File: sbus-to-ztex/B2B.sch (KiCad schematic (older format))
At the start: 6 parts, among them J1 Conn_01x06_Male, J3 Conn_02x07_Odd_Even

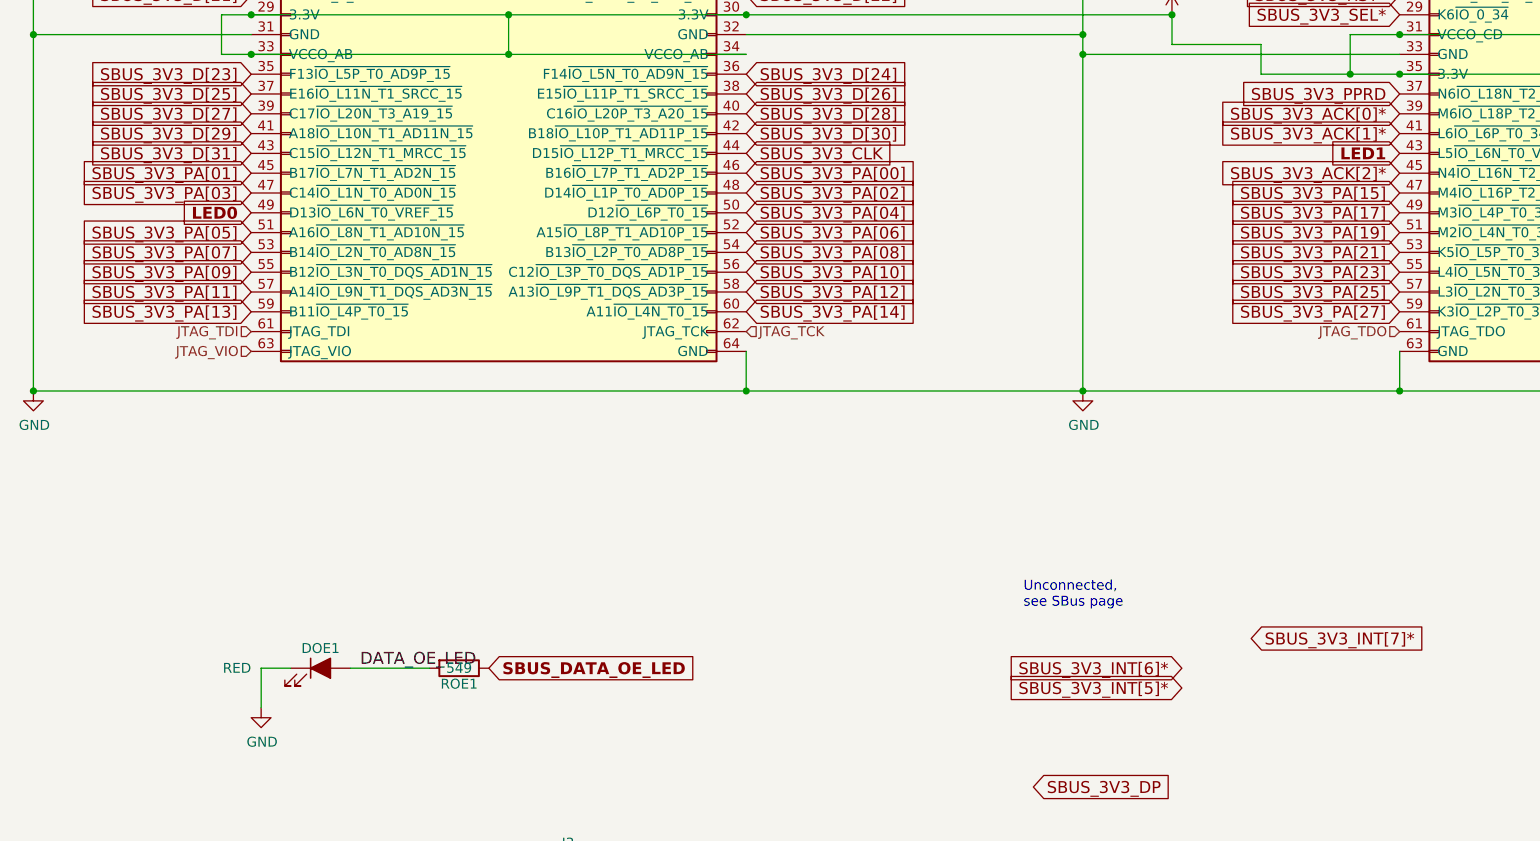
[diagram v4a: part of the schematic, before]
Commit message: Fewer LEDs, more interrupts, replace USB VBus power chip by something that might be available..., update signals file
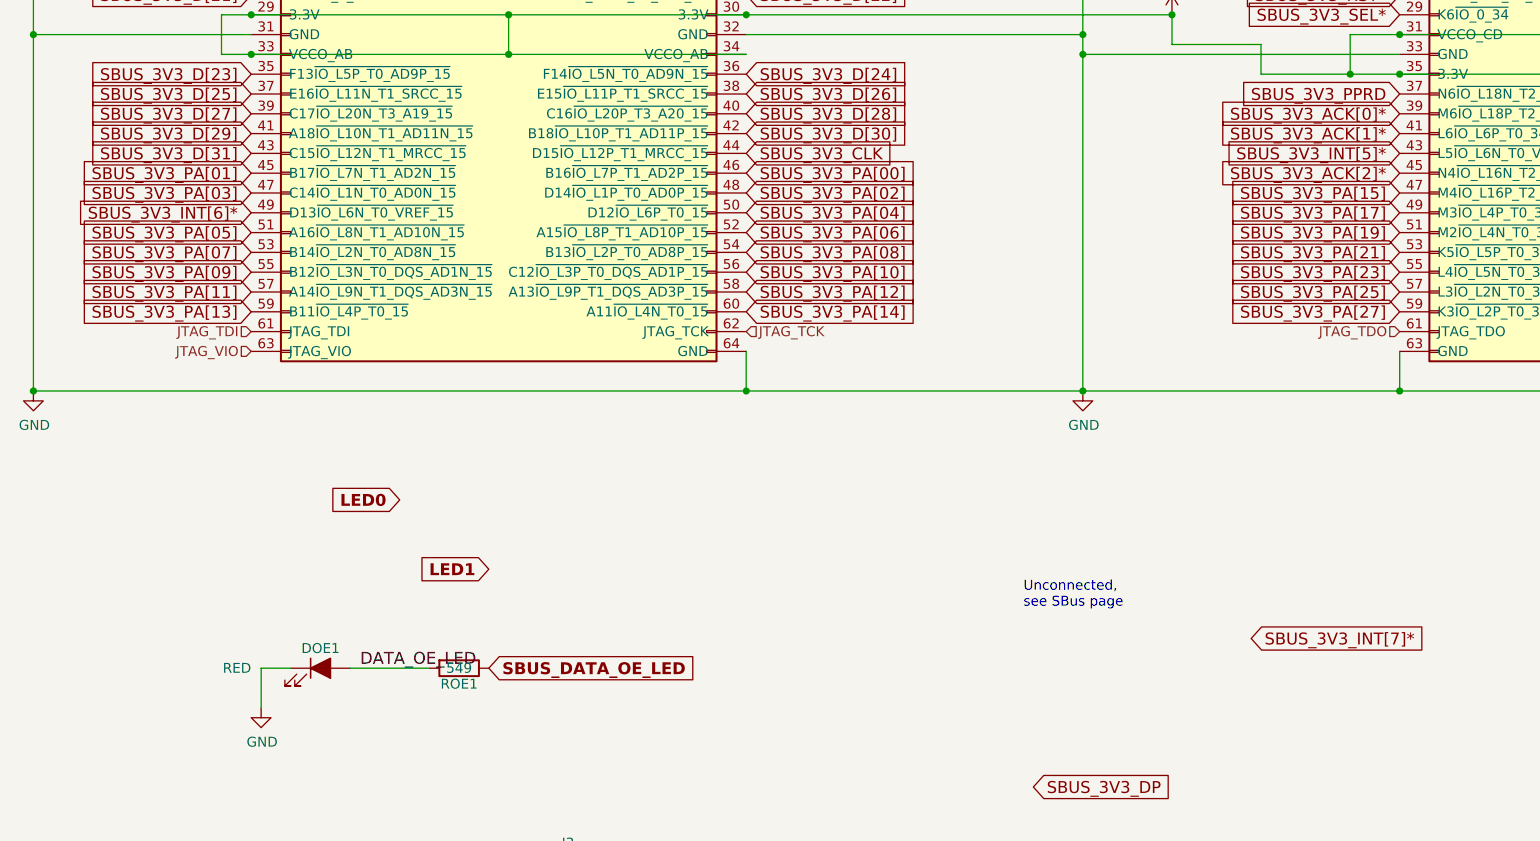
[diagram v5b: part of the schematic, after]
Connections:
- net LED0: no longer JAB1.49 (D13~IO_L6N_T0_VREF_15)
- net LED1: no longer JCD1.43 (L5~IO_L6N_T0_VREF_34)
- net SBUS_3V3_INT[5]*: now also JCD1.43 (L5~IO_L6N_T0_VREF_34)
- net SBUS_3V3_INT[6]*: now also JAB1.49 (D13~IO_L6N_T0_VREF_15)
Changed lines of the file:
@@
 Text GLabel 6650 5700 2    60   Input ~ 0
 SBUS_3V3_INT[7]*
-Text GLabel 6300 5850 0    60   Input ~ 0
+Text GLabel 1600 3550 0    60   Input ~ 0
 SBUS_3V3_INT[6]*
-Text GLabel 6300 5950 0    60   Input ~ 0
+Text GLabel 7400 3250 0    60   Input ~ 0
 SBUS_3V3_INT[5]*
 Text GLabel 9900 3050 2    60   Input ~ 0
@@
 Text GLabel 7400 1750 0    50   Input ~ 0
 PMOD-11
-Text GLabel 1600 3550 0    60   Input ~ 12
+Text GLabel 2350 5000 0    60   Input ~ 12
 LED0
-Text GLabel 7400 3250 0    60   Input ~ 12
+Text GLabel 2800 5350 0    60   Input ~ 12
 LED1
 $EndSCHEMATC

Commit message: Update more stuff to V1.2
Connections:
- net SBUS_3V3_EER*: now also JAB1.49 (D13~IO_L6N_T0_VREF_15); no longer JCD1.25 (V2~IO_L9N_T1_DQS_34)
- net SBUS_3V3_INT[6]*: now also JCD1.25 (V2~IO_L9N_T1_DQS_34); no longer JAB1.49 (D13~IO_L6N_T0_VREF_15)
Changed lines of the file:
@@
 Text GLabel 6650 5700 2    60   Input ~ 0
 SBUS_3V3_INT[7]*
-Text GLabel 1600 3550 0    60   Input ~ 0
+Text GLabel 7400 2350 0    60   Input ~ 0
 SBUS_3V3_INT[6]*
 Text GLabel 7400 3250 0    60   Input ~ 0
@@
 Text GLabel 7400 2950 0    60   Input ~ 0
 SBUS_3V3_PPRD
-Text GLabel 7400 2350 0    60   Input ~ 0
+Text GLabel 1600 3550 0    60   Input ~ 0
 SBUS_3V3_EER*
 Wire Wire Line

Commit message: thinking about a V1.3
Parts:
- removed DOE1: RED, LED_SMD:LED_0805_2012Metric, symbol Device:LED_ALT
- removed J1: Conn_01x06_Male, For_SeeedStudio:PinHeader_1x06_P2.54mm_Horizontal_For_SeeedStudio, symbol Connector:Conn_01x06_Male
- removed ROE1: 549, Resistor_SMD:R_0603_1608Metric, symbol Device:R
- added C24, C8: 100nF 0402, Capacitor_SMD:C_0402_1005Metric, symbol Device:C
- added C6: 47uF 0805, Capacitor_SMD:C_0805_2012Metric, symbol Device:C
- J3: DNP (none) -> DNP
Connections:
- net PMOD-10 is gone; now on net SD_D2: JCD1.42 (P4~IO_L14P_T2_SRCC_34)
- net PMOD-11 is gone; now on net SBUS_3V3_INT[5]*: JCD1.13 (T8~IO_L24N_T3_34)
- net PMOD-12 is gone; now on net SBUS_3V3_INT[4]*: JCD1.11 (U6~IO_L22N_T3_34)
- net PMOD-5 is gone; now on net SD_CLK: JCD1.48 (R1~IO_L17P_T2_34)
- net PMOD-6 is gone; now on net SBUS_3V3_D[23]: JCD1.28 (T3~IO_L11N_T1_SRCC_34)
- net PMOD-7 is gone; now on net SD_CMD: JCD1.46 (T1~IO_L17N_T2_34)
- net PMOD-9 is gone; now on net SD_D3: JCD1.44 (P3~IO_L14N_T2_SRCC_34)
- net RX is gone; now on net USBH0_D+: JCD1.5 (U9~IO_L21P_T3_DQS_34)
- net SBUS_DATA_OE_LED is gone; now on net SBUS_3V3_D[17]: JCD1.26 (U1~IO_L7P_T1_34)
- net TX is gone; now on net USBH0_D-: JCD1.6 (V9~IO_L21N_T3_DQS_34)
- net +3V3: now also C24.1, C8.1
- net +5V: now also C6.1
- net GND: now also C24.2, C6.2, C8.2
- net SBUS_3V3_ACK[0]*: now also JAB1.48 (D14~IO_L1P_T0_AD0P_15); no longer JCD1.39 (M6~IO_L18P_T2_34)
- net SBUS_3V3_ACK[1]*: now also JCD1.56 (N1~IO_L3N_T0_DQS_34); no longer JCD1.41 (L6~IO_L6P_T0_34)
- net SBUS_3V3_ACK[2]*: now also JAB1.57 (A14~IO_L9N_T1_DQS_AD3N_15); no longer JCD1.45 (N4~IO_L16N_T2_34)
- net SBUS_3V3_AS*: now also JAB1.11 (H15~IO_L19N_T3_A21_VREF_15); no longer JCD1.18 (T4~IO_L12N_T1_MRCC_34)
- net SBUS_3V3_BG*: now also JAB1.7 (K15~IO_L24P_T3_RS1_15); no longer JCD1.17 (R7~IO_L23P_T3_34)
- net SBUS_3V3_BR*: now also JAB1.5 (K16~IO_25_15); no longer JCD1.21 (R6~IO_L19P_T3_34)
- net SBUS_3V3_CLK: now also JAB1.20 (H16~IO_L13P_T2_MRCC_15); no longer JAB1.44 (D15~IO_L12P_T1_MRCC_15)
- net SBUS_3V3_D[00]: now also JCD1.17 (R7~IO_L23P_T3_34); no longer JAB1.6 (J18~IO_L23N_T3_FWE_B_15)
- net SBUS_3V3_D[01]: now also JAB1.13 (J14~IO_L19P_T3_A22_15); no longer JAB1.5 (K16~IO_25_15)
- net SBUS_3V3_D[02]: now also JAB1.14 (H14~IO_L15P_T2_DQS_15); no longer JAB1.8 (J17~IO_L23P_T3_FOE_B_15)
- net SBUS_3V3_D[03]: now also JCD1.19 (T6~IO_L23N_T3_34); no longer JAB1.7 (K15~IO_L24P_T3_RS1_15)
- net SBUS_3V3_D[04]: now also JAB1.15 (H17~IO_L18P_T2_A24_15); no longer JAB1.10 (K13~IO_L17P_T2_A26_15)
- net SBUS_3V3_D[05]: now also JAB1.16 (G14~IO_L15N_T2_DQS_ADV_B_15); no longer JAB1.9 (J15~IO_L24N_T3_RS0_15)
- net SBUS_3V3_D[06]: now also JCD1.21 (R6~IO_L19P_T3_34); no longer JAB1.12 (J13~IO_L17N_T2_A25_15)
- net SBUS_3V3_D[07]: now also JAB1.17 (G17~IO_L18N_T2_A23_15); no longer JAB1.13 (J14~IO_L19P_T3_A22_15)
- net SBUS_3V3_D[08]: now also JAB1.18 (G16~IO_L13N_T2_MRCC_15); no longer JAB1.14 (H14~IO_L15P_T2_DQS_15)
- net SBUS_3V3_D[09]: now also JCD1.23 (R5~IO_L19N_T3_VREF_34); no longer JAB1.15 (H17~IO_L18P_T2_A24_15)
- net SBUS_3V3_D[10]: now also JAB1.19 (G18~IO_L22P_T3_A17_15); no longer JAB1.16 (G14~IO_L15N_T2_DQS_ADV_B_15)
- net SBUS_3V3_D[11]: now also JCD1.24 (V1~IO_L7N_T1_34); no longer JAB1.17 (G17~IO_L18N_T2_A23_15)
- net SBUS_3V3_D[12]: now also JAB1.21 (F18~IO_L22N_T3_A16_15); no longer JAB1.18 (G16~IO_L13N_T2_MRCC_15)
- net SBUS_3V3_D[13]: now also JAB1.22 (F16~IO_L14N_T2_SRCC_15); no longer JAB1.19 (G18~IO_L22P_T3_A17_15)
- net SBUS_3V3_D[14]: now also JCD1.25 (V2~IO_L9N_T1_DQS_34); no longer JAB1.20 (H16~IO_L13P_T2_MRCC_15)
- net SBUS_3V3_D[15]: now also JAB1.23 (E18~IO_L21P_T3_DQS_15); no longer JAB1.21 (F18~IO_L22N_T3_A16_15)
- net SBUS_3V3_D[16]: now also JAB1.24 (F15~IO_L14P_T2_SRCC_15); no longer JAB1.22 (F16~IO_L14N_T2_SRCC_15)
- net SBUS_3V3_D[17]: no longer JAB1.23 (E18~IO_L21P_T3_DQS_15)
- net SBUS_3V3_D[18]: now also JAB1.25 (D18~IO_L21N_T3_DQS_A18_15); no longer JAB1.24 (F15~IO_L14P_T2_SRCC_15)
- net SBUS_3V3_D[19]: now also JAB1.26 (E17~IO_L16P_T2_A28_15); no longer JAB1.25 (D18~IO_L21N_T3_DQS_A18_15)
- net SBUS_3V3_D[20]: now also JCD1.27 (U2~IO_L9P_T1_DQS_34); no longer JAB1.26 (E17~IO_L16P_T2_A28_15)
- net SBUS_3V3_D[23]: no longer JAB1.35 (F13~IO_L5P_T0_AD9P_15)
- net SBUS_3V3_D[24]: now also JCD1.29 (K6~IO_0_34); no longer JAB1.36 (F14~IO_L5N_T0_AD9N_15)
- net SBUS_3V3_D[25]: now also JCD1.30 (R3~IO_L11P_T1_SRCC_34); no longer JAB1.37 (E16~IO_L11N_T1_SRCC_15)
- net SBUS_3V3_D[26]: now also JCD1.38 (P5~IO_L13N_T2_MRCC_34); no longer JAB1.38 (E15~IO_L11P_T1_SRCC_15)
- net SBUS_3V3_D[27]: now also JCD1.37 (N6~IO_L18N_T2_34); no longer JAB1.39 (C17~IO_L20N_T3_A19_15)
- net SBUS_3V3_D[28]: now also JCD1.39 (M6~IO_L18P_T2_34); no longer JAB1.40 (C16~IO_L20P_T3_A20_15)
- net SBUS_3V3_D[29]: now also JCD1.41 (L6~IO_L6P_T0_34); no longer JAB1.41 (A18~IO_L10N_T1_AD11N_15)
- net SBUS_3V3_D[30]: now also JAB1.35 (F13~IO_L5P_T0_AD9P_15); no longer JAB1.42 (B18~IO_L10P_T1_AD11P_15)
- net SBUS_3V3_D[31]: now also JAB1.36 (F14~IO_L5N_T0_AD9N_15); no longer JAB1.43 (C15~IO_L12N_T1_MRCC_15)
- net SBUS_3V3_EER*: now also JAB1.43 (C15~IO_L12N_T1_MRCC_15); no longer JAB1.49 (D13~IO_L6N_T0_VREF_15)
- net SBUS_3V3_INT[1]*: now also JAB1.9 (J15~IO_L24N_T3_RS0_15); no longer JCD1.23 (R5~IO_L19N_T3_VREF_34)
- net SBUS_3V3_INT[2]*: now also JCD1.7 (U8~IO_25_34); no longer JAB1.11 (H15~IO_L19N_T3_A21_VREF_15)
- net SBUS_3V3_INT[3]*: now also JCD1.9 (U7~IO_L22P_T3_34); no longer JCD1.30 (R3~IO_L11P_T1_SRCC_34)
- net SBUS_3V3_INT[4]*: no longer JCD1.40 (N5~IO_L13P_T2_MRCC_34)
- net SBUS_3V3_INT[5]*: no longer JCD1.43 (L5~IO_L6N_T0_VREF_34)
- net SBUS_3V3_INT[6]*: now also JCD1.15 (R8~IO_L24P_T3_34); no longer JCD1.25 (V2~IO_L9N_T1_DQS_34)
- net SBUS_3V3_PA[00]: now also JAB1.40 (C16~IO_L20P_T3_A20_15); no longer JAB1.46 (B16~IO_L7P_T1_AD2P_15)
- net SBUS_3V3_PA[01]: now also JAB1.39 (C17~IO_L20N_T3_A19_15); no longer JAB1.45 (B17~IO_L7N_T1_AD2N_15)
- net SBUS_3V3_PA[02]: now also JAB1.41 (A18~IO_L10N_T1_AD11N_15); no longer JAB1.48 (D14~IO_L1P_T0_AD0P_15)
- net SBUS_3V3_PA[03]: now also JCD1.47 (M4~IO_L16P_T2_34); no longer JAB1.47 (C14~IO_L1N_T0_AD0N_15)
- net SBUS_3V3_PA[04]: now also JCD1.49 (M3~IO_L4P_T0_34); no longer JAB1.50 (D12~IO_L6P_T0_15)
- net SBUS_3V3_PA[05]: now also JAB1.42 (B18~IO_L10P_T1_AD11P_15); no longer JAB1.51 (A16~IO_L8N_T1_AD10N_15)
- net SBUS_3V3_PA[06]: now also JCD1.51 (M2~IO_L4N_T0_34); no longer JAB1.52 (A15~IO_L8P_T1_AD10P_15)
- net SBUS_3V3_PA[07]: now also JAB1.44 (D15~IO_L12P_T1_MRCC_15); no longer JAB1.53 (B14~IO_L2N_T0_AD8N_15)
- net SBUS_3V3_PA[08]: now also JAB1.46 (B16~IO_L7P_T1_AD2P_15); no longer JAB1.54 (B13~IO_L2P_T0_AD8P_15)
- net SBUS_3V3_PA[09]: now also JAB1.45 (B17~IO_L7N_T1_AD2N_15); no longer JAB1.55 (B12~IO_L3N_T0_DQS_AD1N_15)
- net SBUS_3V3_PA[10]: now also JAB1.47 (C14~IO_L1N_T0_AD0N_15); no longer JAB1.56 (C12~IO_L3P_T0_DQS_AD1P_15)
- net SBUS_3V3_PA[11]: now also JCD1.53 (K5~IO_L5P_T0_34); no longer JAB1.57 (A14~IO_L9N_T1_DQS_AD3N_15)
- net SBUS_3V3_PA[12]: now also JAB1.49 (D13~IO_L6N_T0_VREF_15); no longer JAB1.58 (A13~IO_L9P_T1_DQS_AD3P_15)
- net SBUS_3V3_PA[13]: now also JCD1.54 (N2~IO_L3P_T0_DQS_34); no longer JAB1.59 (B11~IO_L4P_T0_15)
- net SBUS_3V3_PA[14]: now also JCD1.55 (L4~IO_L5N_T0_34); no longer JAB1.60 (A11~IO_L4N_T0_15)
- net SBUS_3V3_PA[15]: now also JAB1.50 (D12~IO_L6P_T0_15); no longer JCD1.47 (M4~IO_L16P_T2_34)
- net SBUS_3V3_PA[16]: now also JAB1.52 (A15~IO_L8P_T1_AD10P_15); no longer JCD1.50 (R2~IO_L15N_T2_DQS_34)
- net SBUS_3V3_PA[17]: now also JAB1.51 (A16~IO_L8N_T1_AD10N_15); no longer JCD1.49 (M3~IO_L4P_T0_34)
- net SBUS_3V3_PA[18]: now also JAB1.54 (B13~IO_L2P_T0_AD8P_15); no longer JCD1.52 (P2~IO_L15P_T2_DQS_34)
- net SBUS_3V3_PA[19]: now also JAB1.53 (B14~IO_L2N_T0_AD8N_15); no longer JCD1.51 (M2~IO_L4N_T0_34)
- net SBUS_3V3_PA[20]: now also JAB1.55 (B12~IO_L3N_T0_DQS_AD1N_15); no longer JCD1.54 (N2~IO_L3P_T0_DQS_34)
- net SBUS_3V3_PA[21]: now also JCD1.57 (L3~IO_L2N_T0_34); no longer JCD1.53 (K5~IO_L5P_T0_34)
- net SBUS_3V3_PA[22]: now also JCD1.58 (M1~IO_L1N_T0_34); no longer JCD1.56 (N1~IO_L3N_T0_DQS_34)
- net SBUS_3V3_PA[23]: now also JAB1.56 (C12~IO_L3P_T0_DQS_AD1P_15); no longer JCD1.55 (L4~IO_L5N_T0_34)
- net SBUS_3V3_PA[24]: now also JCD1.59 (K3~IO_L2P_T0_34); no longer JCD1.58 (M1~IO_L1N_T0_34)
- net SBUS_3V3_PA[25]: now also JAB1.58 (A13~IO_L9P_T1_DQS_AD3P_15); no longer JCD1.57 (L3~IO_L2N_T0_34)
- net SBUS_3V3_PA[26]: now also JAB1.60 (A11~IO_L4N_T0_15); no longer JCD1.60 (L1~IO_L1P_T0_34)
- net SBUS_3V3_PA[27]: now also JAB1.59 (B11~IO_L4P_T0_15); no longer JCD1.59 (K3~IO_L2P_T0_34)
- net SBUS_3V3_PPRD: now also JAB1.38 (E15~IO_L11P_T1_SRCC_15); no longer JCD1.37 (N6~IO_L18N_T2_34)
- net SBUS_3V3_RST*: now also JCD1.60 (L1~IO_L1P_T0_34); no longer JCD1.27 (U2~IO_L9P_T1_DQS_34)
- net SBUS_3V3_SEL*: now also JAB1.12 (J13~IO_L17N_T2_A25_15); no longer JCD1.29 (K6~IO_0_34)
- net SBUS_3V3_SIZ[0]: now also JAB1.37 (E16~IO_L11N_T1_SRCC_15); no longer JCD1.19 (T6~IO_L23N_T3_34)
- net SBUS_3V3_SIZ[1]: now also JCD1.43 (L5~IO_L6N_T0_VREF_34); no longer JCD1.22 (U3~IO_L8N_T1_34)
- net SBUS_3V3_SIZ[2]: now also JCD1.45 (N4~IO_L16N_T2_34); no longer JCD1.24 (V1~IO_L7N_T1_34)
- net SBUS_OE: now also JAB1.10 (K13~IO_L17P_T2_A26_15); no longer JCD1.38 (P5~IO_L13N_T2_MRCC_34)
- net SD_CLK: no longer JCD1.15 (R8~IO_L24P_T3_34)
- net SD_CMD: no longer JCD1.16 (T5~IO_L12P_T1_MRCC_34)
- net SD_D0: now also JCD1.50 (R2~IO_L15N_T2_DQS_34); no longer JCD1.12 (V5~IO_L10P_T1_34)
- net SD_D1: now also JCD1.52 (P2~IO_L15P_T2_DQS_34); no longer JCD1.14 (V4~IO_L10N_T1_34)
- net SD_D2: no longer JCD1.8 (V7~IO_L20P_T3_34)
- net SD_D3: no longer JCD1.10 (V6~IO_L20N_T3_34)
- net USBH0_D+: no longer JCD1.7 (U8~IO_25_34)
- net USBH0_D-: no longer JCD1.9 (U7~IO_L22P_T3_34)
- net PMOD-8 renamed HDMI_CLK+
- new net CLK_54_000: JCD1.40 (N5~IO_L13P_T2_MRCC_34)
- new net HDMI_CLK-: JCD1.22 (U3~IO_L8N_T1_34)
- new net HDMI_D0+: JCD1.16 (T5~IO_L12P_T1_MRCC_34)
- new net HDMI_D0-: JCD1.18 (T4~IO_L12N_T1_MRCC_34)
- new net HDMI_D1+: JCD1.12 (V5~IO_L10P_T1_34)
- new net HDMI_D1-: JCD1.14 (V4~IO_L10N_T1_34)
- new net HDMI_D2+: JCD1.8 (V7~IO_L20P_T3_34)
- new net HDMI_D2-: JCD1.10 (V6~IO_L20N_T3_34)
- new net I2C0_SCL: JAB1.8 (J17~IO_L23P_T3_FOE_B_15)
- new net I2C0_SDA: JAB1.6 (J18~IO_L23N_T3_FWE_B_15)
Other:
- note removed: "Unconnected,\nsee SBus page"

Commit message: more V1.3
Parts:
- JAB1, JCD1: DNP (none) -> DNP
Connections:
- net labels added: PMOD-1112+, PMOD-1112-, PMOD-56+, PMOD-56-, PMOD-78+, PMOD-78-, PMOD-910+, PMOD-910-
- net labels removed: SBUS_3V3_INT[1]*, SBUS_3V3_INT[6]*
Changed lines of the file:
@@
 F 4 "10-89-7642" H 1800 2650 50  0001 C CNN "MPN"
 F 5 "https://www2.mouser.com/ProductDetail/Molex/10-89-7642?qs=%2Fha2pyFadugCxzQFZUdvioDcljDVidgd4vXrOFuSRYM%3D" H 1800 2650 50  0001 C CNN "URL"
+F 6 "DNP" H 1800 2650 50  0001 C CNN "DNP"
 	1    1800 2650
 	1    0    0    -1
@@
 Text Notes 9950 6500 0    50   ~ 0
 Clock capable inputs (MRCC and SRCC, MRCC are multi-domain)\nFor 2.13:\nB9 G16~IO_L13N_T2_MRCC_15 G16\nB10 H16~IO_L13P_T2_MRCC_15 H16\nB11 F16~IO_L14N_T2_SRCC_15 F16\nB12 F15~IO_L14P_T2_SRCC_15 F15\nA19 E16~IO_L11N_T1_SRCC_15 E16\nB19 E15~IO_L11P_T1_SRCC_15 E15\nA22 C15~IO_L12N_T1_MRCC_15 C15\nB22 D15~IO_L12P_T1_MRCC_15 D15\nD8 T5~IO_L12P_T1_MRCC_34 T5\nD9 T4~IO_L12N_T1_MRCC_34 T4\nD14 T3~IO_L11N_T1_SRCC_34 T3\nD15 R3~IO_L11P_T1_SRCC_34 R3\nD19 P5~IO_L13N_T2_MRCC_34 P5\nD20 N5~IO_L13P_T2_MRCC_34 N5\nD21 P4~IO_L14P_T2_SRCC_34 P4\nD22 P3~IO_L14N_T2_SRCC_34 P3\n\nUnfortunately various 2.1x modules have different clock assignment. B22 hsould be a P-side MRCC for 2.14 (perhaps 2.18), but is a n-side SRCC on 2.16 so not usable there.
-Text GLabel 4100 2050 2    60   Input ~ 0
-SBUS_3V3_CLK
 Wire Wire Line
 	1450 2550 1450 2750
@@
 Wire Wire Line
 	7150 2850 6700 2850
-Text GLabel 7400 1950 0    60   Input ~ 0
-SBUS_3V3_D[00]
-Text GLabel 1600 1750 0    60   Input ~ 0
-SBUS_3V3_D[01]
-Text GLabel 4100 1750 2    60   Input ~ 0
-SBUS_3V3_D[02]
-Text GLabel 7400 2050 0    60   Input ~ 0
-SBUS_3V3_D[03]
-Text GLabel 1600 1850 0    60   Input ~ 0
-SBUS_3V3_D[04]
-Text GLabel 4100 1850 2    60   Input ~ 0
-SBUS_3V3_D[05]
-Text GLabel 7400 2150 0    60   Input ~ 0
-SBUS_3V3_D[06]
-Text GLabel 1600 1950 0    60   Input ~ 0
-SBUS_3V3_D[07]
+Text GLabel 1600 2150 0    60   Input ~ 0
+SBUS_3V3_D[14]
+Text GLabel 4100 1950 2    60   Input ~ 0
+SBUS_3V3_D[09]
+Text GLabel 1600 2050 0    60   Input ~ 0
+SBUS_3V3_D[11]
 Text GLabel 1600 2250 0    60   Input ~ 0
-SBUS_3V3_D[15]
-Text GLabel 7400 2350 0    60   Input ~ 0
-SBUS_3V3_D[14]
-Text GLabel 4100 2150 2    60   Input ~ 0
-SBUS_3V3_D[13]
-Text GLabel 1600 2150 0    60   Input ~ 0
-SBUS_3V3_D[12]
-Text GLabel 7400 2250 0    60   Input ~ 0
-SBUS_3V3_D[09]
-Text GLabel 4100 1950 2    60   Input ~ 0
-SBUS_3V3_D[08]
-Text GLabel 9900 2250 2    60   Input ~ 0
-SBUS_3V3_D[11]
-Text GLabel 1600 2050 0    60   Input ~ 0
-SBUS_3V3_D[10]
-Text GLabel 4100 2250 2    60   Input ~ 0
-SBUS_3V3_D[16]
-Text GLabel 9900 2350 2    60   Input ~ 0
 SBUS_3V3_D[17]
 Text GLabel 1600 2350 0    60   Input ~ 0
-SBUS_3V3_D[18]
-Text GLabel 4100 2350 2    60   Input ~ 0
-SBUS_3V3_D[19]
-Text GLabel 7400 2450 0    60   Input ~ 0
 SBUS_3V3_D[20]
 Text GLabel 1600 2450 0    60   Input ~ 0
-SBUS_3V3_D[21]
-Text GLabel 4100 2450 2    60   Input ~ 0
-SBUS_3V3_D[22]
-Text GLabel 9900 2450 2    60   Input ~ 0
 SBUS_3V3_D[23]
 Text GLabel 4100 2850 2    60   Input ~ 0
@@
 Text GLabel 1600 2850 0    60   Input ~ 0
 SBUS_3V3_D[30]
-Text GLabel 7400 3150 0    60   Input ~ 0
+Text GLabel 9900 2950 2    60   Input ~ 0
 SBUS_3V3_D[29]
-Text GLabel 7400 3050 0    60   Input ~ 0
-SBUS_3V3_D[28]
-Text GLabel 7400 2950 0    60   Input ~ 0
+Text GLabel 9900 2550 2    60   Input ~ 0
 SBUS_3V3_D[27]
-Text GLabel 9900 2950 2    60   Input ~ 0
+Text GLabel 7400 2550 0    60   Input ~ 0
 SBUS_3V3_D[26]
-Text GLabel 9900 2550 2    60   Input ~ 0
+Text GLabel 9900 2450 2    60   Input ~ 0
 SBUS_3V3_D[25]
-Text GLabel 7400 2550 0    60   Input ~ 0
+Text GLabel 4100 2450 2    60   Input ~ 0
 SBUS_3V3_D[24]
-Text GLabel 7400 1850 0    60   Input ~ 0
-SBUS_3V3_INT[6]*
 Text GLabel 7400 1750 0    60   Input ~ 0
 SBUS_3V3_INT[5]*
@@
 Text GLabel 7400 1450 0    60   Input ~ 0
 SBUS_3V3_INT[2]*
-Text GLabel 1600 1550 0    60   Input ~ 0
-SBUS_3V3_INT[1]*
 Text GLabel 4100 3050 2    60   Input ~ 0
 SBUS_3V3_PA[00]
@@
 Text GLabel 1600 3150 0    60   Input ~ 0
 SBUS_3V3_PA[02]
+Text GLabel 7400 3250 0    60   Input ~ 0
+SBUS_3V3_PA[03]
+Text GLabel 7400 3350 0    60   Input ~ 0
+SBUS_3V3_PA[04]
 Text GLabel 7400 3450 0    60   Input ~ 0
-SBUS_3V3_PA[03]
-Text GLabel 7400 3550 0    60   Input ~ 0
-SBUS_3V3_PA[04]
-Text GLabel 7400 3650 0    60   Input ~ 0
 SBUS_3V3_PA[06]
 Text GLabel 4100 3250 2    60   Input ~ 0
@@
 Text GLabel 4100 3550 2    60   Input ~ 0
 SBUS_3V3_PA[15]
-Text GLabel 7400 3850 0    60   Input ~ 0
+Text GLabel 7400 3750 0    60   Input ~ 0
 SBUS_3V3_PA[14]
-Text GLabel 9900 3750 2    60   Input ~ 0
+Text GLabel 7400 3650 0    60   Input ~ 0
 SBUS_3V3_PA[13]
 Text GLabel 1600 3550 0    60   Input ~ 0
 SBUS_3V3_PA[12]
-Text GLabel 7400 3750 0    60   Input ~ 0
+Text GLabel 7400 3550 0    60   Input ~ 0
 SBUS_3V3_PA[11]
 Text GLabel 1600 3450 0    60   Input ~ 0
@@
 Text GLabel 1600 2950 0    60   Input ~ 0
 SBUS_3V3_SIZ[0]
-Text GLabel 7400 3250 0    60   Input ~ 0
+Text GLabel 7400 3050 0    60   Input ~ 0
 SBUS_3V3_SIZ[1]
-Text GLabel 7400 3350 0    60   Input ~ 0
+Text GLabel 7400 3150 0    60   Input ~ 0
 SBUS_3V3_SIZ[2]
 Text GLabel 1600 1350 0    60   Input ~ 0
 SBUS_3V3_BR*
-Text GLabel 4100 1650 2    60   Input ~ 0
-SBUS_3V3_SEL*
 Text GLabel 1600 1450 0    60   Input ~ 0
 SBUS_3V3_BG*
-Text GLabel 1600 1650 0    60   Input ~ 0
-SBUS_3V3_AS*
 Text GLabel 1600 3950 0    60   Input ~ 0
 SBUS_3V3_ACK[2]*
-Text GLabel 9900 3850 2    60   Input ~ 0
+Text GLabel 7400 3850 0    60   Input ~ 0
 SBUS_3V3_ACK[1]*
 Text GLabel 4100 3450 2    60   Input ~ 0
@@
 Text GLabel 1600 3250 0    60   Input ~ 0
 SBUS_3V3_EER*
-Text GLabel 9900 3150 2    60   Input ~ 0
+Text GLabel 12225 3225 2    60   Input ~ 0
 SD_D2
-Text GLabel 9900 3250 2    60   Input ~ 0
+Text GLabel 12225 3325 2    60   Input ~ 0
 SD_D3
-Text GLabel 9900 3350 2    60   Input ~ 0
+Text GLabel 12225 3425 2    60   Input ~ 0
 SD_CMD
-Text GLabel 9900 3450 2    60   Input ~ 0
+Text GLabel 12225 3525 2    60   Input ~ 0
 SD_CLK
-Text GLabel 9900 3550 2    60   Input ~ 0
+Text GLabel 12225 3625 2    60   Input ~ 0
 SD_D0
-Text GLabel 9900 3650 2    60   Input ~ 0
+Text GLabel 12225 3725 2    60   Input ~ 0
 SD_D1
 $Comp
@@
 F 4 "10-89-7642" H 7600 2650 50  0001 C CNN "MPN"
 F 5 "https://www2.mouser.com/ProductDetail/Molex/10-89-7642?qs=%2Fha2pyFadugCxzQFZUdvioDcljDVidgd4vXrOFuSRYM%3D" H 7600 2650 50  0001 C CNN "URL"
+F 6 "DNP" H 7600 2650 50  0001 C CNN "DNP"
 	1    7600 2650
 	1    0    0    -1
@@
 Wire Wire Line
 	500  2650 1600 2650
-Wire Wire Line
-	1600 1250 4100 1250
-Wire Wire Line
-	1600 1250 500  1250
 Wire Wire Line
 	500  1250 500  2650
@@
 Text GLabel 9900 3050 2    50   Input Italic 0
 CLK_54_000
+Wire Wire Line
+	1600 1250 550  1250
+Wire Wire Line
+	1600 1250 4100 1250
+Text GLabel 1600 1550 0    60   Input ~ 0
+SBUS_3V3_AS*
+Text GLabel 4100 2350 2    60   Input ~ 0
+SBUS_3V3_D[21]
+Text GLabel 4100 2250 2    60   Input ~ 0
+SBUS_3V3_D[18]
+Text GLabel 7400 2150 0    60   Input ~ 0
+SBUS_3V3_D[10]
+Text GLabel 7400 2250 0    60   Input ~ 0
+SBUS_3V3_D[12]
+Text GLabel 4100 2150 2    60   Input ~ 0
+SBUS_3V3_D[15]
+Text GLabel 7400 2050 0    60   Input ~ 0
+SBUS_3V3_D[07]
+Text GLabel 7400 1950 0    60   Input ~ 0
+SBUS_3V3_D[04]
+Text GLabel 7400 1850 0    60   Input ~ 0
+SBUS_3V3_D[01]
+Text GLabel 7400 2950 0    60   Input ~ 0
+SBUS_3V3_D[28]
+Text GLabel 1600 1650 0    60   Input ~ 0
+SBUS_3V3_SEL*
+Text GLabel 7400 2450 0    60   Input ~ 0
+SBUS_3V3_D[22]
+Text GLabel 9900 2350 2    60   Input ~ 0
+SBUS_3V3_D[19]
+Text GLabel 7400 2350 0    60   Input ~ 0
+SBUS_3V3_D[16]
+Text GLabel 9900 2250 2    60   Input ~ 0
+SBUS_3V3_D[13]
+Text GLabel 1600 1850 0    60   Input ~ 0
+SBUS_3V3_D[05]
+Text GLabel 1600 1750 0    60   Input ~ 0
+SBUS_3V3_D[02]
+Text GLabel 4100 2050 2    60   Input ~ 0
+SBUS_3V3_CLK
+Text GLabel 1600 1950 0    60   Input ~ 0
+SBUS_3V3_D[08]
+Text GLabel 4100 1850 2    60   Input ~ 0
+SBUS_3V3_D[06]
+Text GLabel 4100 1750 2    60   Input ~ 0
+SBUS_3V3_D[03]
+Text GLabel 4100 1650 2    60   Input ~ 0
+SBUS_3V3_D[00]
+Text GLabel 9900 3850 2    50   Input ~ 0
+PMOD-56-
+Text GLabel 9900 3550 2    50   Input ~ 0
+PMOD-78-
+Text GLabel 9900 3350 2    50   Input ~ 0
+PMOD-910-
+Text GLabel 9900 3250 2    50   Input ~ 0
+PMOD-1112-
+Text GLabel 9900 3150 2    50   Input ~ 0
+PMOD-1112+
+Text GLabel 9900 3750 2    50   Input ~ 0
+PMOD-56+
+Text GLabel 9900 3650 2    50   Input ~ 0
+PMOD-78+
+Text GLabel 9900 3450 2    50   Input ~ 0
+PMOD-910+
 $EndSCHEMATC
